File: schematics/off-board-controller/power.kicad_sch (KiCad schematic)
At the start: 4 parts, among them J3 xt60, U6 L78L33_TO92

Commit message: off-board: created schematic
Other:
- title: (none) -> Off-board Controller
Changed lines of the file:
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@@
 	(generator_version "8.0")
 	(paper "A4")
+	(title_block
+		(title "Off-board Controller")
+		(date "2024-07-20")
+	)
 	(junction
 		(at 119.38 83.82)

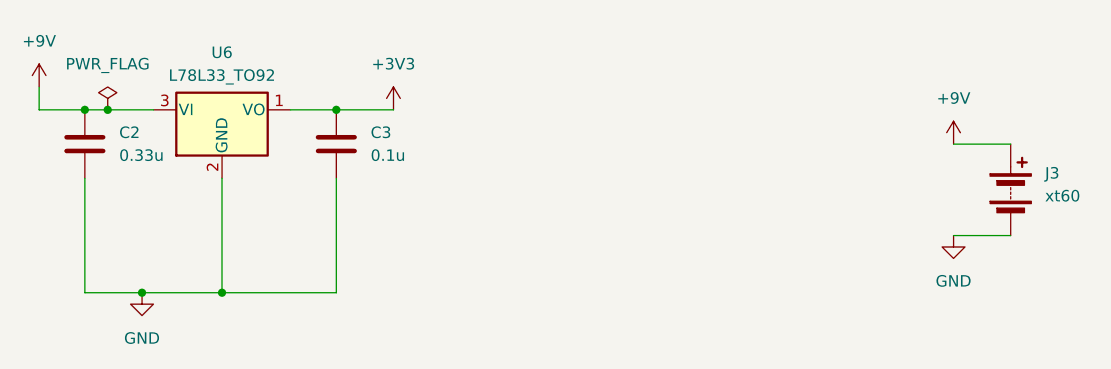
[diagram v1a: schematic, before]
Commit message: finished footprints, schematic, and started layout
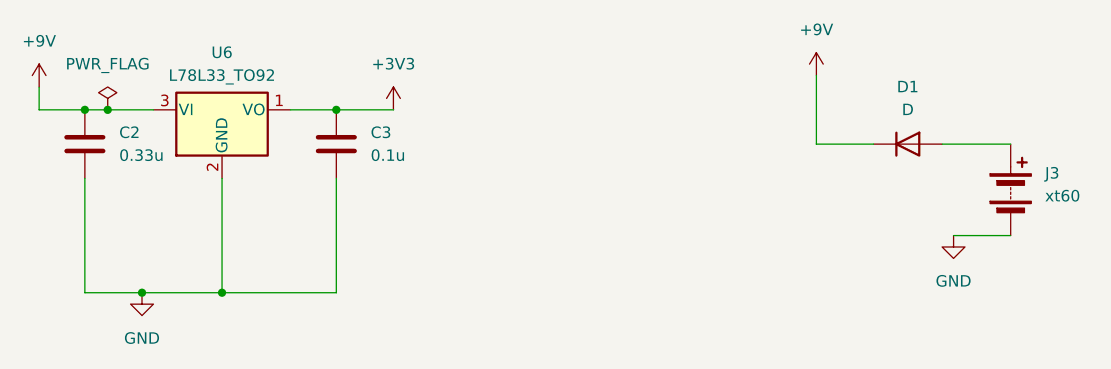
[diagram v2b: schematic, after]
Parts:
- added D1: D, LED_SMD:LED_0805_2012Metric_Pad1.15x1.40mm_HandSolder, symbol Device:D
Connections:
- net +9V: now also D1.1 (K); no longer J3.1 (+)
- new net: D1.2 (A), J3.1 (+)
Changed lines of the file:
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@@
+	(wire
+		(pts
+			(xy 200.66 87.63) (xy 207.01 87.63)
+		)
+		(stroke
+			(width 0)
+			(type default)
+		)
+	)
 	(wire
 		(pts
@@
 	(wire
 		(pts
+			(xy 200.66 80.01) (xy 200.66 87.63)
+		)
+		(stroke
+			(width 0)
+			(type default)
+		)
+	)
+	(wire
+		(pts
 			(xy 119.38 83.82) (xy 114.3 83.82)
 		)
@@
 	(wire
 		(pts
-			(xy 215.9 87.63) (xy 222.25 87.63)
-		)
-		(stroke
-			(width 0)
-			(type default)
-		)
-	)
-	(wire
-		(pts
 			(xy 121.92 83.82) (xy 119.38 83.82)
 		)
@@
 		(pts
 			(xy 215.9 97.79) (xy 222.25 97.79)
+		)
+		(stroke
+			(width 0)
+			(type default)
+		)
+	)
+	(wire
+		(pts
+			(xy 214.63 87.63) (xy 222.25 87.63)
 		)
 		(stroke
@@
 	(symbol
 		(lib_id "power:+9V")
-		(at 215.9 87.63 0)
+		(at 200.66 80.01 0)
 		(unit 1)
 		(exclude_from_sim no)
@@
 		(fields_autoplaced yes)
 		(property "Reference" "#PWR09"
-			(at 215.9 91.44 0)
+			(at 200.66 83.82 0)
 			(effects
 				(font
@@
 		)
 		(property "Value" "+9V"
-			(at 215.9 82.55 0)
+			(at 200.66 74.93 0)
 			(effects
 				(font
@@
 		)
 		(property "Footprint" ""
-			(at 215.9 87.63 0)
+			(at 200.66 80.01 0)
 			(effects
 				(font
@@
 		)
 		(property "Datasheet" ""
-			(at 215.9 87.63 0)
+			(at 200.66 80.01 0)
 			(effects
 				(font
@@
 		)
 		(property "Description" "Power symbol creates a global label with name \"+9V\""
-			(at 215.9 87.63 0)
+			(at 200.66 80.01 0)
 			(effects
 				(font
@@
 					(unit 1)
 				)
+			)
+		)
+	)
+	(symbol
+		(lib_id "Device:D")
+		(at 210.82 87.63 0)
+		(unit 1)
+		(exclude_from_sim no)
+		(in_bom yes)
+		(on_board yes)
+		(dnp no)
+		(fields_autoplaced yes)
+		(property "Reference" "D1"
+			(at 210.82 81.28 0)
+			(effects
+				(font
+					(size 1.27 1.27)
+				)
+			)
+		)
+		(property "Value" "D"
+			(at 210.82 83.82 0)
+			(effects
+				(font
+					(size 1.27 1.27)
+				)
+			)
+		)
+		(property "Footprint" "LED_SMD:LED_0805_2012Metric_Pad1.15x1.40mm_HandSolder"
+			(at 210.82 87.63 0)
+			(effects
+				(font
+					(size 1.27 1.27)
+				)
+				(hide yes)
+			)
+		)
+		(property "Datasheet" "~"
+			(at 210.82 87.63 0)
+			(effects
+				(font
+					(size 1.27 1.27)
+				)
+				(hide yes)
+			)
+		)
+		(property "Description" "Diode"
+			(at 210.82 87.63 0)
+			(effects
+				(font
+					(size 1.27 1.27)
+				)
+				(hide yes)
+			)
+		)
+		(property "Sim.Device" "D"
+			(at 210.82 87.63 0)
+			(effects
+				(font
+					(size 1.27 1.27)
+				)
+				(hide yes)
+			)
+		)
+		(property "Sim.Pins" "1=K 2=A"
+			(at 210.82 87.63 0)
+			(effects
+				(font
+					(size 1.27 1.27)
+				)
+				(hide yes)
+			)
+		)
+		(pin "2"
+		)
+		(pin "1"
+		)
+		(instances
+			(project "controller"
+				(path "/0775f04a-8a0e-41f5-b442-dacb2efdb863/c3c1d3dc-6187-4a85-b6a0-9f3d8dc916f4"
+					(reference "D1")
+					(unit 1)
+				)

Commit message: produced first draft of layout design
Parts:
- J3: value xt60 -> 9V
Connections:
- net batt: now reaches D1.2 (A), J3.1 (+)
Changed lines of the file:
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@@
+		)
+	)
+	(label "batt"
+		(at 220.98 87.63 0)
+		(fields_autoplaced yes)
+		(effects
+			(font
+				(size 1.27 1.27)
+			)
+			(justify left bottom)
 		)
 	)
@@
 			)
 		)
-		(property "Value" "xt60"
+		(property "Value" "9V"
 			(at 226.06 93.4084 0)
 			(effects

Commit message: submitted version for checking
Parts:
- D1: footprint LED_SMD:LED_0805_2012Metric_Pad1.15x1.40mm_HandSolder -> Diode_THT:D_A-405_P7.62mm_Horizontal
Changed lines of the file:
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@@
 			)
 		)
-		(property "Footprint" "LED_SMD:LED_0805_2012Metric_Pad1.15x1.40mm_HandSolder"
+		(property "Footprint" "Diode_THT:D_A-405_P7.62mm_Horizontal"
 			(at 210.82 87.63 0)
 			(effects
